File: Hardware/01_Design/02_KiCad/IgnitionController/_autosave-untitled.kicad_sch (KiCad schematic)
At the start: 34 parts, among them Q4 PMOS-FET, Q5 BC856, Q6 IRF9Z34NSPbF, U3 LM2575-3.3BU, U4 LM2575-5.0BU, U9 LM2575-5.0BU

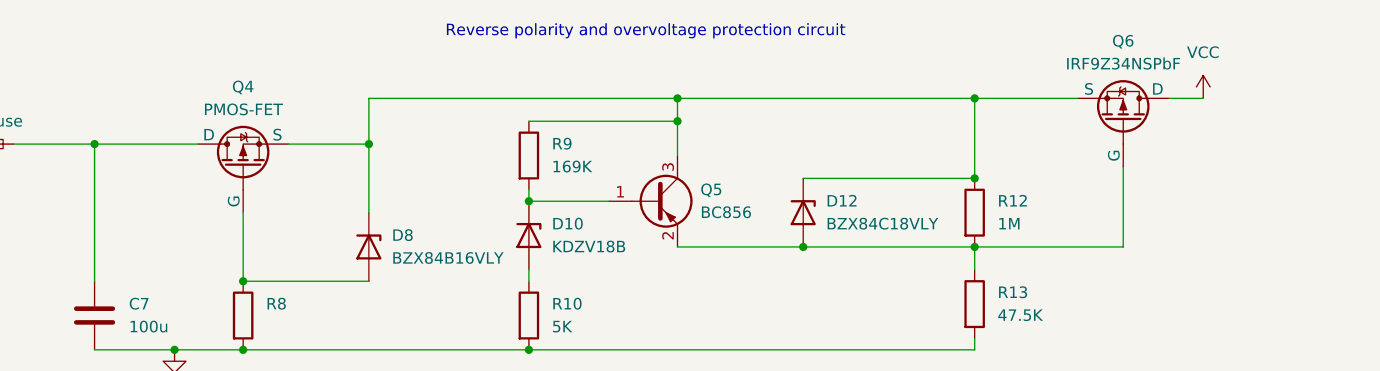
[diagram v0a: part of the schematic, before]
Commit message: Initial routing of Power supply
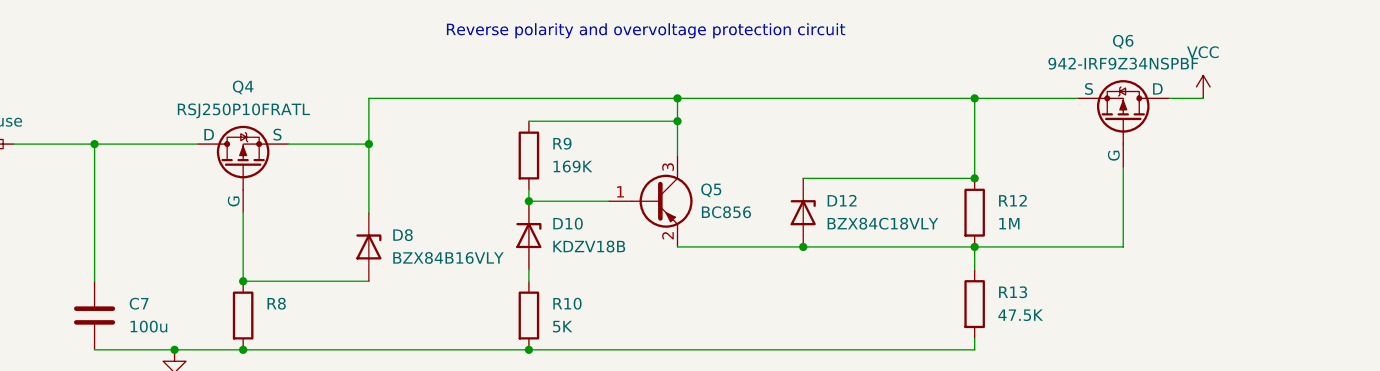
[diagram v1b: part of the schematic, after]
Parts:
- removed Q6: IRF9Z34NSPbF, Package_TO_SOT_SMD:TO-263-2, symbol Simulation_SPICE:PMOS
- added Q6: 942-IRF9Z34NSPBF, Library:TO-263-2_Transistor, symbol Library_sym.pretty:PMOS-FET
- C7: footprint Capacitor_SMD:C_0805_2012Metric_Pad1.18x1.45mm_HandSolder -> Capacitor_SMD:C_0603_1608Metric_Pad1.08x0.95mm_HandSolder
- Q4: value PMOS-FET -> RSJ250P10FRATL; Mouser PN (none) -> 755-RSJ250P10FRATL
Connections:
- net VCC: now also Q6.2 (D)
- net at D12.3 (K), D8.3 (K), Q4.3 (S)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: now also Q6.3 (S)
- net at D12.1 (A), Q5.2 (E), R12.2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: now also Q6.1 (G)
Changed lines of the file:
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@@
 			)
 		)
-		(property "Value" "PMOS-FET"
+		(property "Value" "RSJ250P10FRATL"
 			(at 87.63 49.53 90)
 			(effects
@@
 			)
 		)
+		(property "Mouser PN" "755-RSJ250P10FRATL"
+			(at 87.63 55.88 90)
+			(effects
+				(font
+					(size 1.27 1.27)
+				)
+				(hide yes)
+			)
+		)
 		(pin "3"
 		)
@@
 			)
 		)
-		(property "Footprint" "Capacitor_SMD:C_0805_2012Metric_Pad1.18x1.45mm_HandSolder"
+		(property "Footprint" "Capacitor_SMD:C_0603_1608Metric_Pad1.08x0.95mm_HandSolder"
 			(at 72.0852 76.2 0)
 			(effects
@@
 	)
 	(symbol
-		(lib_id "Simulation_SPICE:PMOS")
-		(at 185.42 50.8 270)
-		(mirror x)
-		(unit 1)
-		(exclude_from_sim no)
-		(in_bom yes)
-		(on_board yes)
-		(dnp no)
-		(property "Reference" "Q6"
-			(at 185.42 41.91 90)
-			(effects
-				(font
-					(size 1.27 1.27)
-				)
-			)
-		)
-		(property "Value" "IRF9Z34NSPbF"
-			(at 185.42 44.45 90)
-			(effects
-				(font
-					(size 1.27 1.27)
-				)
-			)
-		)
-		(property "Footprint" "Package_TO_SOT_SMD:TO-263-2"
-			(at 187.96 45.72 0)
-			(effects
-				(font
-					(size 1.27 1.27)
-				)
-				(hide yes)
-			)
-		)
-		(property "Datasheet" "https://ngspice.sourceforge.io/docs/ngspice-html-manual/manual.xhtml#cha_MOSFETs"
-			(at 172.72 50.8 0)
-			(effects
-				(font
-					(size 1.27 1.27)
-				)
-				(hide yes)
-			)
-		)
-		(property "Description" "P-MOSFET transistor, drain/source/gate"
-			(at 185.42 50.8 0)
-			(effects
-				(font
-					(size 1.27 1.27)
-				)
-				(hide yes)
-			)
-		)
-		(property "Sim.Device" "PMOS"
-			(at 168.275 50.8 0)
-			(effects
-				(font
-					(size 1.27 1.27)
-				)
-				(hide yes)
-			)
-		)
-		(property "Sim.Type" "VDMOS"
-			(at 166.37 50.8 0)
-			(effects
-				(font
-					(size 1.27 1.27)
-				)
-				(hide yes)
-			)
-		)
-		(property "Sim.Pins" "1=D 2=G 3=S"
-			(at 170.18 50.8 0)
-			(effects
-				(font
-					(size 1.27 1.27)
-				)
-				(hide yes)
-			)
-		)
-		(pin "2"
-		)
-		(pin "1"
-		)
-		(pin "3"
-		)
-		(instances
-			(project "IgnitionController"
-				(path "/96744ec0-1e7f-4d75-9985-0095978419e2/af36972c-908c-4a23-b0c1-8f51d47880c3"
-					(reference "Q6")
-					(unit 1)
-				)
-			)
-		)
-	)
-	(symbol
 		(lib_id "Diode:SS14")
 		(at 82.55 160.02 270)
@@
 					(unit 1)
 				)
+			)
+		)
+	)
+	(symbol
+		(lib_id "Library_sym.pretty:PMOS-FET")
+		(at 185.42 50.8 270)
+		(mirror x)
+		(unit 1)
+		(exclude_from_sim no)
+		(in_bom yes)
+		(on_board yes)
+		(dnp no)
+		(property "Reference" "Q6"
+			(at 185.42 41.91 90)
+			(effects
+				(font
+					(size 1.27 1.27)
+				)
+			)
+		)
+		(property "Value" "942-IRF9Z34NSPBF"
+			(at 185.42 44.45 90)
+			(effects
+				(font
+					(size 1.27 1.27)
+				)
+			)
+		)
+		(property "Footprint" "Library:TO-263-2_Transistor"
+			(at 187.96 45.72 0)
+			(effects
+				(font
+					(size 1.27 1.27)
+				)
+				(hide yes)
+			)
+		)
+		(property "Datasheet" "https://ngspice.sourceforge.io/docs/ngspice-html-manual/manual.xhtml#cha_MOSFETs"
+			(at 172.72 50.8 0)
+			(effects
+				(font
+					(size 1.27 1.27)
+				)
+				(hide yes)
+			)
+		)
+		(property "Description" "P-MOSFET transistor, drain/source/gate"
+			(at 185.42 50.8 0)
+			(effects
+				(font
+					(size 1.27 1.27)
+				)
+				(hide yes)
+			)
+		)
+		(property "Sim.Device" "PMOS"
+			(at 168.275 50.8 0)
+			(effects
+				(font
+					(size 1.27 1.27)
+				)
+				(hide yes)
+			)
+		)
+		(property "Sim.Type" "VDMOS"
+			(at 166.37 50.8 0)
+			(effects
+				(font
+					(size 1.27 1.27)
+				)
+				(hide yes)
+			)
+		)
+		(property "Sim.Pins" "1=D 2=G 3=S"
+			(at 170.18 50.8 0)
+			(effects
+				(font
+					(size 1.27 1.27)
+				)
+				(hide yes)
+			)
+		)
+		(property "Mouser PN" ""
+			(at 185.42 50.8 90)
+			(effects
+				(font
+					(size 1.27 1.27)
+				)
+				(hide yes)
+			)
+		)
+		(pin "3"
+		)
+		(pin "1"
+		)
+		(pin "2"
+		)
+		(instances
+			(project "IgnitionController"
+				(path "/96744ec0-1e7f-4d75-9985-0095978419e2/af36972c-908c-4a23-b0c1-8f51d47880c3"
+					(reference "Q6")
+					(unit 1)
+				)
